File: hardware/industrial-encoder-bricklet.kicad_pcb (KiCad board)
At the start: 2 copper layers, 40 x 40 mm, 66 parts, among them P1 CON-SENSOR, P2 Boot, P3 CONN_8, U1 XMC1XXX24, U2 OPA358, U3 ISL32173E, U4 DRILL, U5 DRILL, U6 DRILL, U7 DRILL

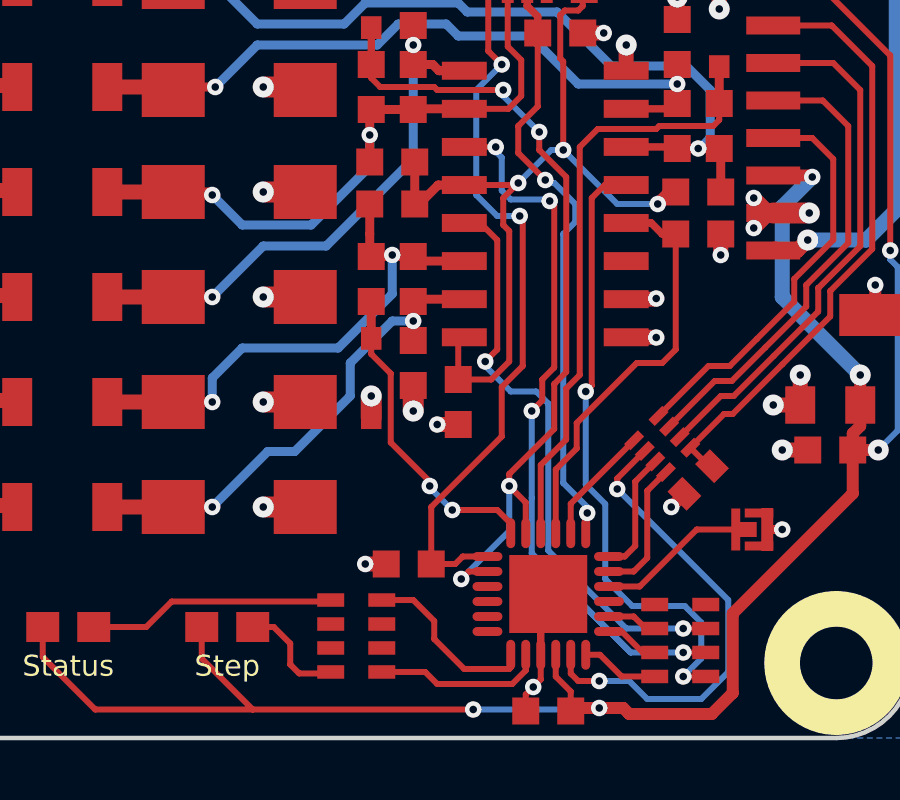
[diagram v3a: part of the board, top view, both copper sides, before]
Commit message: fix 5V connection error of ISL
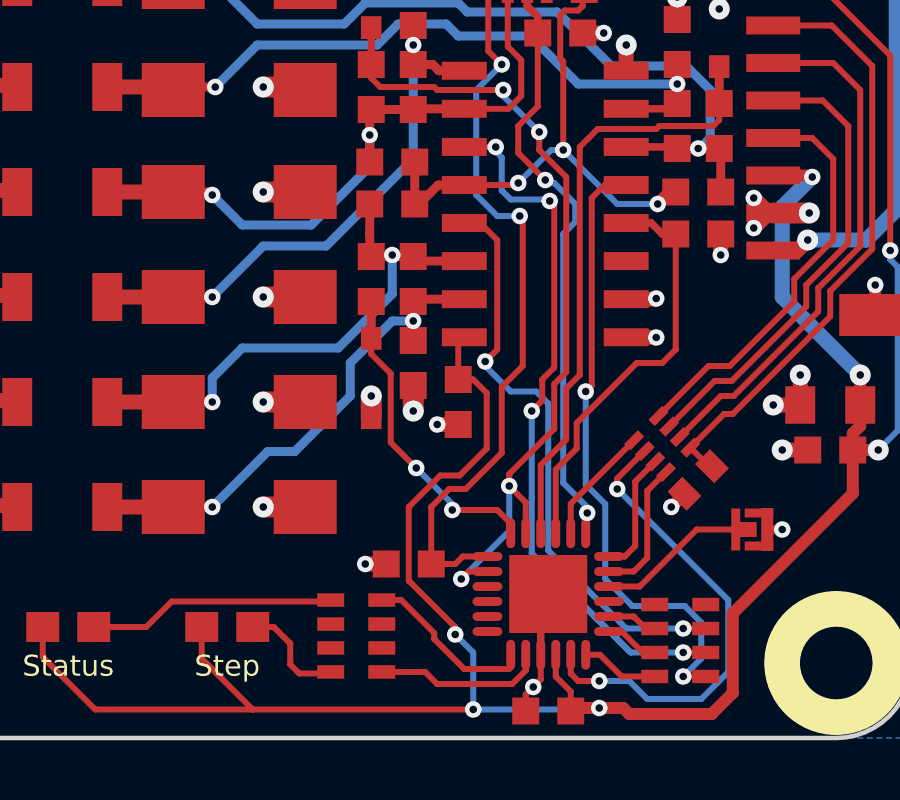
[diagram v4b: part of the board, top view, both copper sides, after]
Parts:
- U2: footprint kicad-libraries:SC70-6 -> SC70-6
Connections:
- C6 pad 1: +5VA -> VCC
- U3 pad 16: +5VA -> VCC
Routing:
- net VCC: track 80.8 -> 96.3 mm, vias 6 -> 7
- net +5VA: track 49.6 -> 39.9 mm
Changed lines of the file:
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@@
     (links 132)
     (no_connects 0)
-    (area 165.544999 85.044999 276.69286 162.45)
+    (area 166.324999 85.824999 206.475001 125.975001)
     (thickness 1.6)
     (drawings 21)
-    (tracks 596)
+    (tracks 603)
     (zones 0)
     (modules 66)
@@
   (layers
     (0 F.Cu signal)
-    (31 B.Cu signal hide)
+    (31 B.Cu signal)
     (32 B.Adhes user hide)
     (33 F.Adhes user hide)
@@
       (net 16 ~I))
     (pad 16 smd rect (at -4.44246 -2.69748 90) (size 0.59944 1.4986) (layers F.Cu F.Paste F.Mask)
-      (net 7 +5VA))
+      (net 2 VCC))
     (model Housings_SOIC/SOIC-16_3.9x9.9mm_Pitch1.27mm.wrl
       (at (xyz 0 0 0))
@@
     (fp_line (start -1.45034 0.65024) (end -1.45034 -0.65024) (layer F.Fab) (width 0.001))
     (pad 1 smd rect (at -0.75 0 270) (size 0.9 0.9) (layers F.Cu F.Paste F.Mask)
-      (net 7 +5VA))
+      (net 2 VCC))
     (pad 2 smd rect (at 0.75 0 270) (size 0.9 0.9) (layers F.Cu F.Paste F.Mask)
       (net 1 GND))
@@
       (net 7 +5VA))
   )
-  (module kicad-libraries:SC70-6 (layer F.Cu)
+  (module SC70-6 (layer F.Cu)
     (at 193.6 100.1 180)
     (fp_text reference U2 (at 0.3 0.2 180) (layer F.Fab)
@@
   (segment (start 193.642283 120.976093) (end 193.642284 122.276095) (width 0.2) (layer F.Cu) (net 1))
   (segment (start 194.942283 120.976092) (end 193.642283 120.976093) (width 0.2) (layer F.Cu) (net 1))
+  (segment (start 191.3 113.95) (end 191.8 113.95) (width 0.2) (layer F.Cu) (net 2))
+  (segment (start 191.8 123.05) (end 191.8 124.95) (width 0.2) (layer B.Cu) (net 2))
+  (segment (start 191.2 122.45) (end 191.8 123.05) (width 0.2) (layer B.Cu) (net 2))
+  (via (at 191.2 122.45) (size 0.55) (drill 0.25) (layers F.Cu B.Cu) (net 2))
+  (segment (start 191.2 122.205022) (end 191.2 122.45) (width 0.2) (layer F.Cu) (net 2))
+  (segment (start 189.65 120.655022) (end 191.2 122.205022) (width 0.2) (layer F.Cu) (net 2))
+  (segment (start 189.65 118.2) (end 189.65 120.655022) (width 0.2) (layer F.Cu) (net 2))
+  (segment (start 190.7 117.15) (end 189.65 118.2) (width 0.2) (layer F.Cu) (net 2))
+  (segment (start 191.35 117.15) (end 190.7 117.15) (width 0.2) (layer F.Cu) (net 2))
+  (segment (start 192.25 116.25) (end 191.35 117.15) (width 0.2) (layer F.Cu) (net 2))
+  (segment (start 192.25 114.4) (end 192.25 116.25) (width 0.2) (layer F.Cu) (net 2))
+  (segment (start 191.8 113.95) (end 192.25 114.4) (width 0.2) (layer F.Cu) (net 2))
   (segment (start 204.7 113.8) (end 202.1 111.2) (width 0.5) (layer B.Cu) (net 2))
   (segment (start 203.05 107.15) (end 203.1 107.2) (width 0.4) (layer F.Cu) (net 2))
@@
   (segment (start 182.7499 122.2) (end 182.7499 123.2499) (width 0.2) (layer F.Cu) (net 2))
   (segment (start 195.95 124.95) (end 196 124.9) (width 0.2) (layer B.Cu) (net 2))
+  (via (at 196 124.9) (size 0.55) (drill 0.25) (layers F.Cu B.Cu) (net 2))
   (segment (start 191.8 124.95) (end 195.95 124.95) (width 0.2) (layer B.Cu) (net 2))
   (via (at 191.8 124.95) (size 0.55) (drill 0.25) (layers F.Cu B.Cu) (net 2))
-  (via (at 196 124.9) (size 0.55) (drill 0.25) (layers F.Cu B.Cu) (net 2))
   (segment (start 184.45 124.95) (end 191.8 124.95) (width 0.2) (layer F.Cu) (net 2))
   (segment (start 182.7499 123.2499) (end 184.45 124.95) (width 0.2) (layer F.Cu) (net 2))
   (segment (start 196 124.9) (end 195.05 124.9) (width 0.4) (layer F.Cu) (net 2))
+  (segment (start 191.3 113.95) (end 191.3 112.74498) (width 0.2) (layer F.Cu) (net 2))
+  (segment (start 191.3 112.74498) (end 191.50252 112.54246) (width 0.2) (layer F.Cu) (net 2))
   (segment (start 196.325 119.85) (end 196.85 119.85) (width 0.2) (layer F.Cu) (net 3))
   (segment (start 197.2 117.352026) (end 197.869427 116.682599) (width 0.2) (layer F.Cu) (net 3))
@@
   (segment (start 191.50252 107.46754) (end 193.23246 107.46754) (width 0.2) (layer F.Cu) (net 7))
   (segment (start 193.23246 107.46754) (end 193.3 107.4) (width 0.2) (layer F.Cu) (net 7))
-  (segment (start 192.8 107.9) (end 193.3 107.4) (width 0.2) (layer F.Cu) (net 7))
-  (segment (start 192.8 108.8) (end 192.8 107.9) (width 0.2) (layer F.Cu) (net 7))
-  (segment (start 192.399998 113.95) (end 193 113.349998) (width 0.2) (layer F.Cu) (net 7))
-  (segment (start 193 113.349998) (end 193 109) (width 0.2) (layer F.Cu) (net 7))
-  (segment (start 193 109) (end 192.8 108.8) (width 0.2) (layer F.Cu) (net 7))
-  (segment (start 191.3 113.95) (end 192.399998 113.95) (width 0.2) (layer F.Cu) (net 7))
-  (segment (start 191.3 113.95) (end 191.3 112.74498) (width 0.2) (layer F.Cu) (net 7))
-  (segment (start 191.3 112.74498) (end 191.50252 112.54246) (width 0.2) (layer F.Cu) (net 7))
   (segment (start 190.05 90.45) (end 191.15 90.45) (width 0.5) (layer F.Cu) (net 7))
   (segment (start 190.94924 90.24924) (end 191.15 90.45) (width 0.5) (layer F.Cu) (net 7))
@@
   (segment (start 197.6 119.9) (end 197.6 117.659671) (width 0.2) (layer F.Cu) (net 27))
   (segment (start 197.15 120.35) (end 197.6 119.9) (width 0.2) (layer F.Cu) (net 27))
+  (segment (start 192.75 114.2) (end 192.75 116.4) (width 0.2) (layer F.Cu) (net 28))
+  (segment (start 191.55 117.6) (end 191 117.6) (width 0.2) (layer F.Cu) (net 28))
+  (segment (start 192.75 116.4) (end 191.55 117.6) (width 0.2) (layer F.Cu) (net 28))
   (segment (start 192.275 119.85) (end 191.45 119.85) (width 0.2) (layer F.Cu) (net 28))
   (segment (start 191.2 120.1) (end 190.4 120.1) (width 0.2) (layer F.Cu) (net 28))
   (segment (start 191.45 119.85) (end 191.2 120.1) (width 0.2) (layer F.Cu) (net 28))
-  (segment (start 190.4 118.2) (end 192.75 115.85) (width 0.2) (layer F.Cu) (net 28))
+  (segment (start 190.4 118.2) (end 191 117.6) (width 0.2) (layer F.Cu) (net 28))
+  (segment (start 190.4 120.1) (end 190.4 118.2) (width 0.2) (layer F.Cu) (net 28))
   (segment (start 193.45 113.5) (end 193.45 108.6) (width 0.2) (layer F.Cu) (net 28))
   (segment (start 192.75 114.2) (end 193.45 113.5) (width 0.2) (layer F.Cu) (net 28))
-  (segment (start 192.75 115.85) (end 192.75 114.2) (width 0.2) (layer F.Cu) (net 28))
   (segment (start 193.45 108.6) (end 193.35 108.5) (width 0.2) (layer F.Cu) (net 28))
   (via (at 193.35 108.5) (size 0.55) (drill 0.25) (layers F.Cu B.Cu) (net 28))
@@
   (segment (start 192.3 100.4) (end 192.3 103) (width 0.2) (layer F.Cu) (net 28))
   (segment (start 192.95 99.75) (end 192.3 100.4) (width 0.2) (layer F.Cu) (net 28))
-  (segment (start 190.4 120.1) (end 190.4 118.2) (width 0.2) (layer F.Cu) (net 28))
   (segment (start 191.9 104.3) (end 191.9 107.8) (width 0.2) (layer B.Cu) (net 28))
   (segment (start 192.3 103) (end 192.75 103.45) (width 0.2) (layer F.Cu) (net 28))
@@
   (segment (start 188.4 103.9) (end 188.4 103.45) (width 0.2) (layer F.Cu) (net 31))
   (segment (start 188.4 103.45) (end 188.4 102.2208) (width 0.25) (layer F.Cu) (net 31))
+  (segment (start 191.1 118.3) (end 191.1 118.1) (width 0.2) (layer B.Cu) (net 32))
+  (via (at 189.9 116.9) (size 0.55) (drill 0.25) (layers F.Cu B.Cu) (net 32))
+  (segment (start 191.1 118.1) (end 189.9 116.9) (width 0.2) (layer B.Cu) (net 32))
   (segment (start 193.05 119.075) (end 193.05 118.75) (width 0.2) (layer F.Cu) (net 32))
   (segment (start 193.05 118.75) (end 192.6 118.3) (width 0.2) (layer F.Cu) (net 32))
   (segment (start 192.6 118.3) (end 191.1 118.3) (width 0.2) (layer F.Cu) (net 32))
-  (segment (start 189.05 116.05) (end 190.35 117.35) (width 0.2) (layer F.Cu) (net 32))
-  (segment (start 188.4 113.1) (end 189.05 113.75) (width 0.2) (layer F.Cu) (net 32))
+  (segment (start 189.05 116.05) (end 189.9 116.9) (width 0.2) (layer F.Cu) (net 32))
+  (segment (start 189.05 116.05) (end 189.05 113.75) (width 0.2) (layer F.Cu) (net 32))
   (segment (start 188.4 112.5792) (end 188.4 113.1) (width 0.2) (layer F.Cu) (net 32))
+  (segment (start 188.4 113.1) (end 189.05 113.75) (width 0.2) (layer F.Cu) (net 32))
   (via (at 191.1 118.3) (size 0.55) (drill 0.25) (layers F.Cu B.Cu) (net 32))
-  (segment (start 191.1 118.3) (end 190.35 117.55) (width 0.2) (layer B.Cu) (net 32))
-  (segment (start 190.35 117.55) (end 190.35 117.5) (width 0.2) (layer B.Cu) (net 32))
-  (via (at 190.35 117.5) (size 0.55) (drill 0.25) (layers F.Cu B.Cu) (net 32))
-  (segment (start 189.05 116.05) (end 189.05 113.75) (width 0.2) (layer F.Cu) (net 32))
-  (segment (start 190.35 117.35) (end 190.35 117.5) (width 0.2) (layer F.Cu) (net 32))
   (segment (start 188.4 112.5792) (end 188.4 111.35) (width 0.3) (layer F.Cu) (net 32))
   (segment (start 193.05 107.95) (end 194.3 107.95) (width 0.2) (layer B.Cu) (net 33))
@@
   (segment (start 193 123.6) (end 191.5 123.6) (width 0.2) (layer F.Cu) (net 39))
   (segment (start 191.5 123.6) (end 190.5 122.6) (width 0.2) (layer F.Cu) (net 39))
-  (segment (start 190.5 122.6) (end 190.5 122) (width 0.2) (layer F.Cu) (net 39))
-  (segment (start 190.5 122) (end 189.80112 121.30112) (width 0.2) (layer F.Cu) (net 39))
-  (segment (start 189.80112 121.30112) (end 188.7509 121.30112) (width 0.2) (layer F.Cu) (net 39))
+  (segment (start 190.5 122.6) (end 190.5 122.4) (width 0.2) (layer F.Cu) (net 39))
+  (segment (start 190.5 122.4) (end 189.40112 121.30112) (width 0.2) (layer F.Cu) (net 39))
+  (segment (start 189.40112 121.30112) (end 188.7509 121.30112) (width 0.2) (layer F.Cu) (net 39))
   (segment (start 181.80036 90.2) (end 181.80036 93.7) (width 0.5) (layer F.Cu) (net 40))
   (segment (start 181.80036 93.7) (end 179.60114 93.7) (width 0.5) (layer F.Cu) (net 40))

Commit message: Add 3d information (final)
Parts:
- P3: footprint OQ_8P -> kicad-libraries:OQ_8P
- RP1: footprint 4X0402 -> kicad-libraries:4X0402
- U2: footprint SC70-6 -> kicad-libraries:SC70-6
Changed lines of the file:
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@@
-(kicad_pcb (version 4) (host pcbnew 4.0.6-e0-6349~53~ubuntu16.04.1)
+(kicad_pcb (version 4) (host pcbnew 4.0.2+dfsg1-stable)
   (general
     (links 132)
@@
     (pad 2 smd rect (at 0.8501 0) (size 1.1 1) (layers F.Cu F.Paste F.Mask)
       (net 10 "Net-(D2-Pad2)"))
-    (model LED_SMD/D_0603_blue.wrl
+    (model LED_SMD/D_0603_green.wrl
       (at (xyz 0 0 0))
       (scale (xyz 1 1 1))
@@
     )
   )
-  (module OQ_8P (layer F.Cu)
-    (at 174.4 105.9 270)
-    (fp_text reference P3 (at 0 3.98 270) (layer F.Fab)
-      (effects (font (size 0.59944 0.59944) (thickness 0.12446)))
-    )
-    (fp_text value CONN_8 (at 0 3.05054 270) (layer F.Fab)
-      (effects (font (size 0.59944 0.59944) (thickness 0.12446)))
-    )
-    (fp_line (start 0 8.001) (end 14.74978 8.001) (layer F.Fab) (width 0.381))
-    (fp_line (start 14.74978 -1.19888) (end 0 -1.19888) (layer F.Fab) (width 0.381))
-    (fp_line (start -14.74978 -1.19888) (end 0.7493 -1.19888) (layer F.Fab) (width 0.381))
-    (fp_line (start 0.7493 8.001) (end -14.74978 8.001) (layer F.Fab) (width 0.381))
-    (fp_line (start -14.74978 8.001) (end -14.74978 -1.19888) (layer F.Fab) (width 0.381))
-    (fp_line (start 14.74978 -1.19888) (end 14.74978 8.001) (layer F.Fab) (width 0.381))
-    (pad 2 thru_hole circle (at -8.7503 0 270) (size 2.4003 2.4003) (drill 1.39954) (layers *.Cu *.Mask F.SilkS)
-      (net 1 GND))
-    (pad 3 thru_hole circle (at -5.25018 0 270) (size 2.4003 2.4003) (drill 1.39954) (layers *.Cu *.Mask F.SilkS)
-      (net 18 "Net-(P3-Pad3)"))
-    (pad 4 thru_hole circle (at -1.75006 0 270) (size 2.4003 2.4003) (drill 1.39954) (layers *.Cu *.Mask F.SilkS)
-      (net 19 "Net-(P3-Pad4)"))
-    (pad 1 thru_hole circle (at -12.25042 0 270) (size 2.4003 2.4003) (drill 1.39954) (layers *.Cu *.Mask F.SilkS)
-      (net 20 "Net-(P3-Pad1)"))
-    (pad 5 thru_hole circle (at 1.75006 0 270) (size 2.4003 2.4003) (drill 1.39954) (layers *.Cu *.Mask F.SilkS)
-      (net 21 "Net-(P3-Pad5)"))
-    (pad 6 thru_hole circle (at 5.25018 0 270) (size 2.4003 2.4003) (drill 1.39954) (layers *.Cu *.Mask F.SilkS)
-      (net 22 "Net-(P3-Pad6)"))
-    (pad 7 thru_hole circle (at 8.7503 0 270) (size 2.4003 2.4003) (drill 1.39954) (layers *.Cu *.Mask F.SilkS)
-      (net 23 "Net-(P3-Pad7)"))
-    (pad 8 thru_hole circle (at 12.25042 0 270) (size 2.4003 2.4003) (drill 1.39954) (layers *.Cu *.Mask F.SilkS)
-      (net 24 "Net-(P3-Pad8)"))
-  )
   (module R0603F (layer F.Cu)
     (at 189.65 120.1)
@@
     )
   )
-  (module 4X0402 (layer F.Cu)
+  (module R0603F (layer F.Cu)
+    (at 200 105.5 270)
+    (attr smd)
+    (fp_text reference R6 (at 0.05 0.225 270) (layer F.Fab)
+      (effects (font (size 0.2 0.2) (thickness 0.05)))
+    )
+    (fp_text value 100 (at 0.05 -0.375 270) (layer F.Fab)
+      (effects (font (size 0.2 0.2) (thickness 0.05)))
+    )
+    (fp_line (start -1.45034 -0.65024) (end 1.45034 -0.65024) (layer F.Fab) (width 0.001))
+    (fp_line (start 1.45034 -0.65024) (end 1.45034 0.65024) (layer F.Fab) (width 0.001))
+    (fp_line (start 1.45034 0.65024) (end -1.45034 0.65024) (layer F.Fab) (width 0.001))
+    (fp_line (start -1.45034 0.65024) (end -1.45034 -0.65024) (layer F.Fab) (width 0.001))
+    (pad 1 smd rect (at -0.75 0 270) (size 0.9 0.9) (layers F.Cu F.Paste F.Mask)
+      (net 30 A-T))
+    (pad 2 smd rect (at 0.75 0 270) (size 0.9 0.9) (layers F.Cu F.Paste F.Mask)
+      (net 11 A/DAT))
+    (model Resistors_SMD/R_0603.wrl
+      (at (xyz 0 0 0))
+      (scale (xyz 1 1 1))
+      (rotate (xyz 0 0 0))
+    )
+  )
+  (module kicad-libraries:4X0402 (layer F.Cu)
     (at 198.1 116.1 315)
     (attr smd)
@@
     (pad 8 smd rect (at -0.7493 -0.575 315) (size 0.29972 0.65) (layers F.Cu F.Paste F.Mask)
       (net 41 "Net-(P1-Pad4)"))
-  )
-  (module R0603F (layer F.Cu)
-    (at 200 105.5 270)
-    (attr smd)
-    (fp_text reference R6 (at 0.05 0.225 270) (layer F.Fab)
-      (effects (font (size 0.2 0.2) (thickness 0.05)))
-    )
-    (fp_text value 100 (at 0.05 -0.375 270) (layer F.Fab)
-      (effects (font (size 0.2 0.2) (thickness 0.05)))
-    )
-    (fp_line (start -1.45034 -0.65024) (end 1.45034 -0.65024) (layer F.Fab) (width 0.001))
-    (fp_line (start 1.45034 -0.65024) (end 1.45034 0.65024) (layer F.Fab) (width 0.001))
-    (fp_line (start 1.45034 0.65024) (end -1.45034 0.65024) (layer F.Fab) (width 0.001))
-    (fp_line (start -1.45034 0.65024) (end -1.45034 -0.65024) (layer F.Fab) (width 0.001))
-    (pad 1 smd rect (at -0.75 0 270) (size 0.9 0.9) (layers F.Cu F.Paste F.Mask)
-      (net 30 A-T))
-    (pad 2 smd rect (at 0.75 0 270) (size 0.9 0.9) (layers F.Cu F.Paste F.Mask)
-      (net 11 A/DAT))
-    (model Resistors_SMD/R_0603.wrl
+    (model Resistors_SMD/R_4x0402.wrl
       (at (xyz 0 0 0))
       (scale (xyz 1 1 1))
-      (rotate (xyz 0 0 0))
+      (rotate (xyz 0 0 90))
     )
   )
-  (module kicad-libraries:WE-LQ-1210 (layer F.Cu)
-    (at 191.15 91.65 90)
-    (fp_text reference L1 (at 0 0.6 90) (layer F.Fab)
-      (effects (font (size 0.3 0.3) (thickness 0.075)))
-    )
-    (fp_text value 6.8uH (at 0 0 90) (layer F.Fab)
-      (effects (font (size 0.3 0.3) (thickness 0.075)))
-    )
-    (fp_line (start -1.6 -1.3) (end 1.6 -1.3) (layer F.Fab) (width 0.15))
-    (fp_line (start 1.6 -1.3) (end 1.6 1.2) (layer F.Fab) (width 0.15))
-    (fp_line (start 1.6 1.2) (end -1.6 1.2) (layer F.Fab) (width 0.15))
-    (fp_line (start -1.6 1.2) (end -1.6 -1.3) (layer F.Fab) (width 0.15))
-    (pad 1 smd rect (at -1.2 0 90) (size 1.4 2.8) (layers F.Cu F.Paste F.Mask)
-      (net 8 +5V))
-    (pad 2 smd rect (at 1.2 0 90) (size 1.4 2.8) (layers F.Cu F.Paste F.Mask)
-      (net 7 +5VA))
-  )
-  (module SC70-6 (layer F.Cu)
+  (module kicad-libraries:SC70-6 (layer F.Cu)
     (at 193.6 100.1 180)
     (fp_text reference U2 (at 0.3 0.2 180) (layer F.Fab)
@@
     (pad 5 smd rect (at 0 -0.95 180) (size 0.4 0.7) (layers F.Cu F.Paste F.Mask)
       (net 29 B-CLK-EN))
+    (model Housing_SOT_SOD/SOT-363.wrl
+      (at (xyz 0 0 0))
+      (scale (xyz 1 1 1))
+      (rotate (xyz 90 180 0))
+    )
+  )
+  (module kicad-libraries:WE-LQ-1210 (layer F.Cu)
+    (at 191.15 91.65 90)
+    (fp_text reference L1 (at 0 0.6 90) (layer F.Fab)
+      (effects (font (size 0.3 0.3) (thickness 0.075)))
+    )
+    (fp_text value 6.8uH (at 0 0 90) (layer F.Fab)
+      (effects (font (size 0.3 0.3) (thickness 0.075)))
+    )
+    (fp_line (start -1.6 -1.3) (end 1.6 -1.3) (layer F.Fab) (width 0.15))
+    (fp_line (start 1.6 -1.3) (end 1.6 1.2) (layer F.Fab) (width 0.15))
+    (fp_line (start 1.6 1.2) (end -1.6 1.2) (layer F.Fab) (width 0.15))
+    (fp_line (start -1.6 1.2) (end -1.6 -1.3) (layer F.Fab) (width 0.15))
+    (pad 1 smd rect (at -1.2 0 90) (size 1.4 2.8) (layers F.Cu F.Paste F.Mask)
+      (net 8 +5V))
+    (pad 2 smd rect (at 1.2 0 90) (size 1.4 2.8) (layers F.Cu F.Paste F.Mask)
+      (net 7 +5VA))
+    (model Inductors/WE_LQ_1210.wrl
+      (at (xyz 0 0 0))
+      (scale (xyz 1 1 1))
+      (rotate (xyz 0 0 0))
+    )
+  )
+  (module kicad-libraries:OQ_8P (layer F.Cu)
+    (at 174.4 105.9 270)
+    (fp_text reference P3 (at 0 3.98 270) (layer F.Fab)
+      (effects (font (size 0.59944 0.59944) (thickness 0.12446)))
+    )
+    (fp_text value CONN_8 (at 0 3.05054 270) (layer F.Fab)
+      (effects (font (size 0.59944 0.59944) (thickness 0.12446)))
+    )
+    (fp_line (start 0 8.001) (end 14.74978 8.001) (layer F.Fab) (width 0.381))
+    (fp_line (start 14.74978 -1.19888) (end 0 -1.19888) (layer F.Fab) (width 0.381))
+    (fp_line (start -14.74978 -1.19888) (end 0.7493 -1.19888) (layer F.Fab) (width 0.381))
+    (fp_line (start 0.7493 8.001) (end -14.74978 8.001) (layer F.Fab) (width 0.381))
+    (fp_line (start -14.74978 8.001) (end -14.74978 -1.19888) (layer F.Fab) (width 0.381))
+    (fp_line (start 14.74978 -1.19888) (end 14.74978 8.001) (layer F.Fab) (width 0.381))
+    (pad 2 thru_hole circle (at -8.7503 0 270) (size 2.4003 2.4003) (drill 1.39954) (layers *.Cu *.Mask F.SilkS)
+      (net 1 GND))
+    (pad 3 thru_hole circle (at -5.25018 0 270) (size 2.4003 2.4003) (drill 1.39954) (layers *.Cu *.Mask F.SilkS)
+      (net 18 "Net-(P3-Pad3)"))
+    (pad 4 thru_hole circle (at -1.75006 0 270) (size 2.4003 2.4003) (drill 1.39954) (layers *.Cu *.Mask F.SilkS)
+      (net 19 "Net-(P3-Pad4)"))
+    (pad 1 thru_hole circle (at -12.25042 0 270) (size 2.4003 2.4003) (drill 1.39954) (layers *.Cu *.Mask F.SilkS)
+      (net 20 "Net-(P3-Pad1)"))
+    (pad 5 thru_hole circle (at 1.75006 0 270) (size 2.4003 2.4003) (drill 1.39954) (layers *.Cu *.Mask F.SilkS)
+      (net 21 "Net-(P3-Pad5)"))
+    (pad 6 thru_hole circle (at 5.25018 0 270) (size 2.4003 2.4003) (drill 1.39954) (layers *.Cu *.Mask F.SilkS)
+      (net 22 "Net-(P3-Pad6)"))
+    (pad 7 thru_hole circle (at 8.7503 0 270) (size 2.4003 2.4003) (drill 1.39954) (layers *.Cu *.Mask F.SilkS)
+      (net 23 "Net-(P3-Pad7)"))
+    (pad 8 thru_hole circle (at 12.25042 0 270) (size 2.4003 2.4003) (drill 1.39954) (layers *.Cu *.Mask F.SilkS)
+      (net 24 "Net-(P3-Pad8)"))
+    (model Connectors/OQ_8P_green.wrl
+      (at (xyz 0 -0.125 0.14))
+      (scale (xyz 1 1 1))
+      (rotate (xyz 0 0 0))
+    )
   )
   (gr_text "Copyright Tinkerforge GmbH 2017.\nThis documentation describes Open Hardware and is licensed under the\nCERN OHL v. 1.1.\nYou may redistribute and modify this documentation under the terms of the\nCERN OHL v.1.1. (http://ohwr.org/cernohl). This documentation is distributed\nWITHOUT ANY EXPRESS OR IMPLIED WARRANTY, INCLUDING OF\nMERCHANTABILITY, SATISFACTORY QUALITY AND FITNESS FOR A\nPARTICULAR PURPOSE. Please see the CERN OHL v.1.1 for applicable\nconditions" (at 231.8 150.9) (layer Cmts.User)
